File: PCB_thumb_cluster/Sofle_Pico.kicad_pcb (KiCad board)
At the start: 2 copper layers, 50 x 57.5 mm, 9 parts, among them J3 Conn_01x06, SW1 SW_PUSH, SW2 SW_PUSH, SW3 SW_PUSH, SW4 SW_PUSH

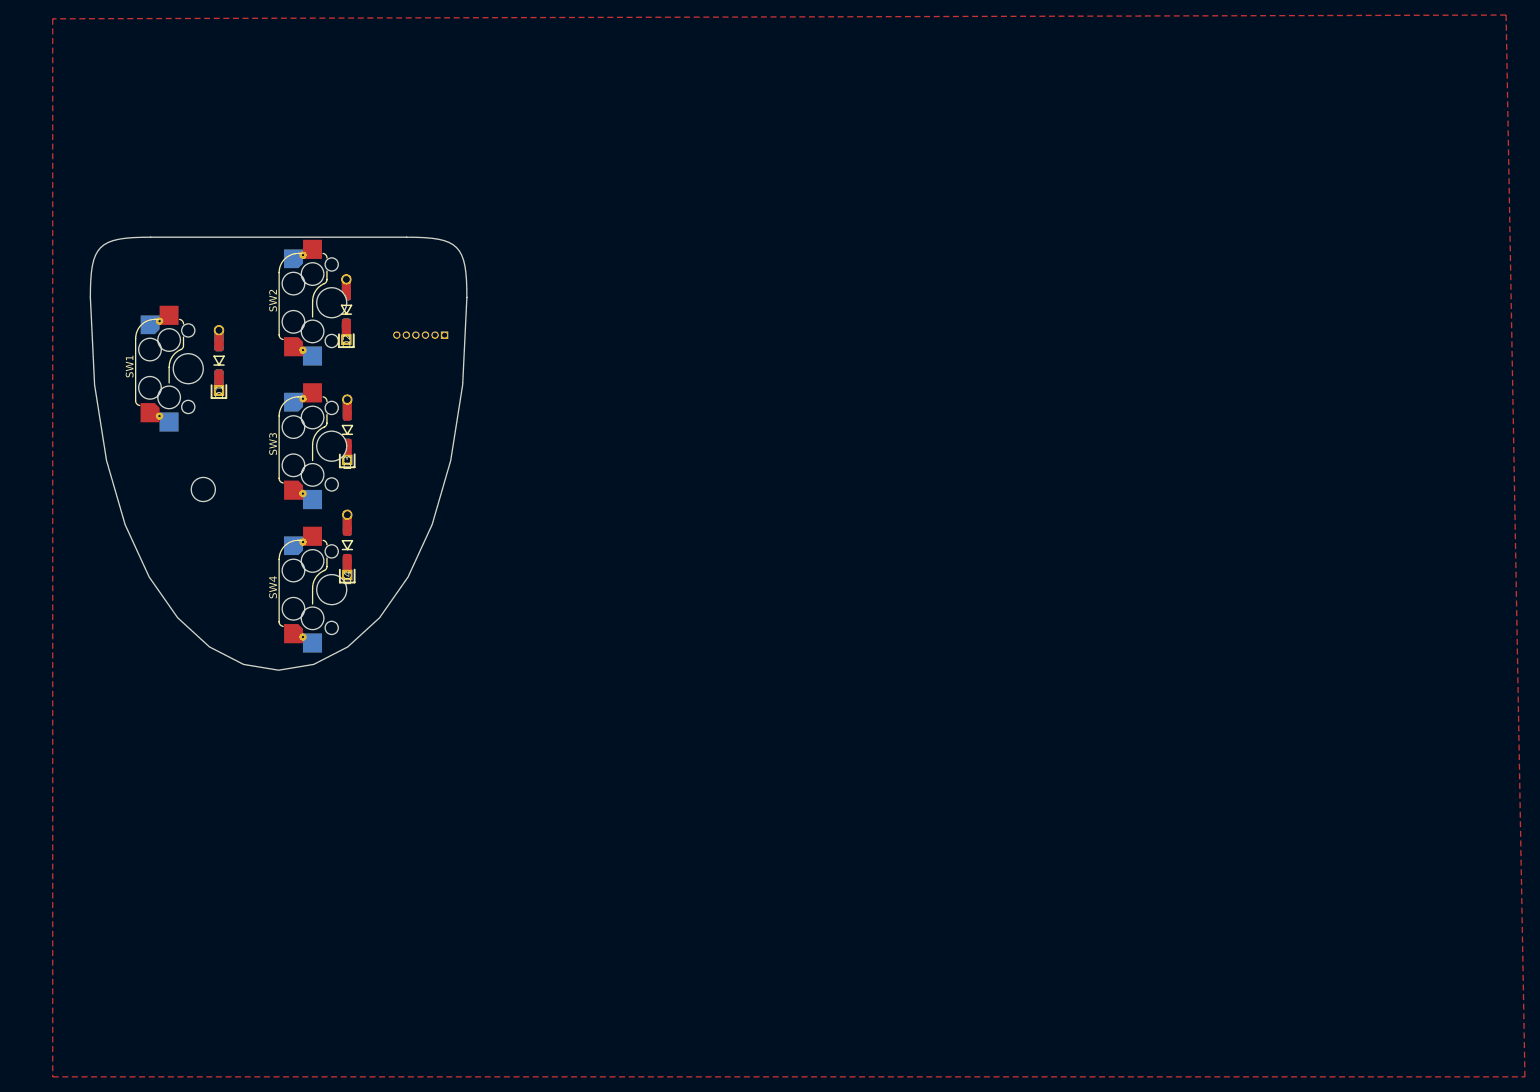
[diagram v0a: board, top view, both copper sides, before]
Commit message: route thumb cluster
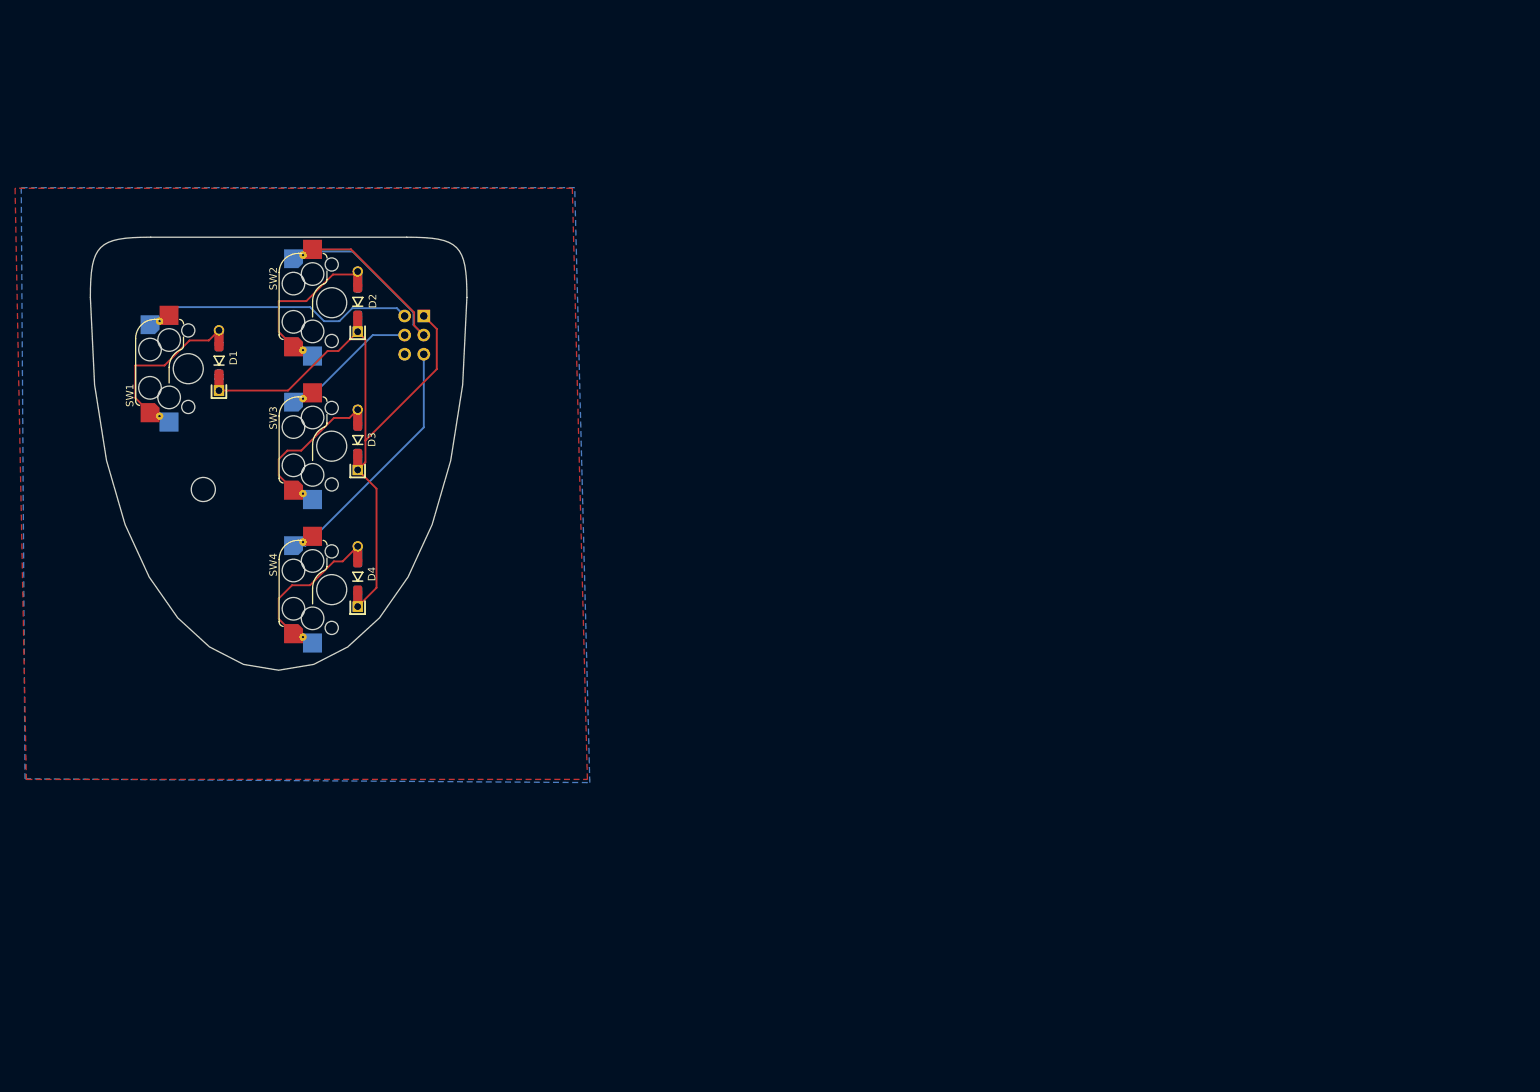
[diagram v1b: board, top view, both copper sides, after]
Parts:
- J3: value Conn_01x06 -> Conn_02x03; footprint Connector_PinHeader_1.27mm:PinHeader_1x06_P1.27mm_Horizontal -> Connector_PinHeader_2.54mm:PinHeader_2x03_P2.54mm_Vertical
- moved D4 4.41 mm to (106.5, 79.0)
- moved J3 3.75 mm to (115.3, 44.5), turned to 180 degrees
- moved D3 1.92 mm to (106.5, 60.9)
- moved D2 1.83 mm to (106.5, 42.5)
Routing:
- net row5: track 0.00 -> 82.3 mm
- net lcol1: track 0.00 -> 42.3 mm
- net lcol0: track 0.00 -> 35.2 mm
- net lcol3: track 0.00 -> 33.5 mm
- net Net-(D1-A): track 0.00 -> 20.1 mm
- net Net-(D2-A): track 0.00 -> 19.0 mm
- net Net-(D4-A): track 0.00 -> 18.8 mm
- net Net-(D3-A): track 0.00 -> 18.1 mm
- net lcol2: track 0.00 -> 17.0 mm
- added copper zone on B.Cu, net (none)
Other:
- board text removed: "USB"

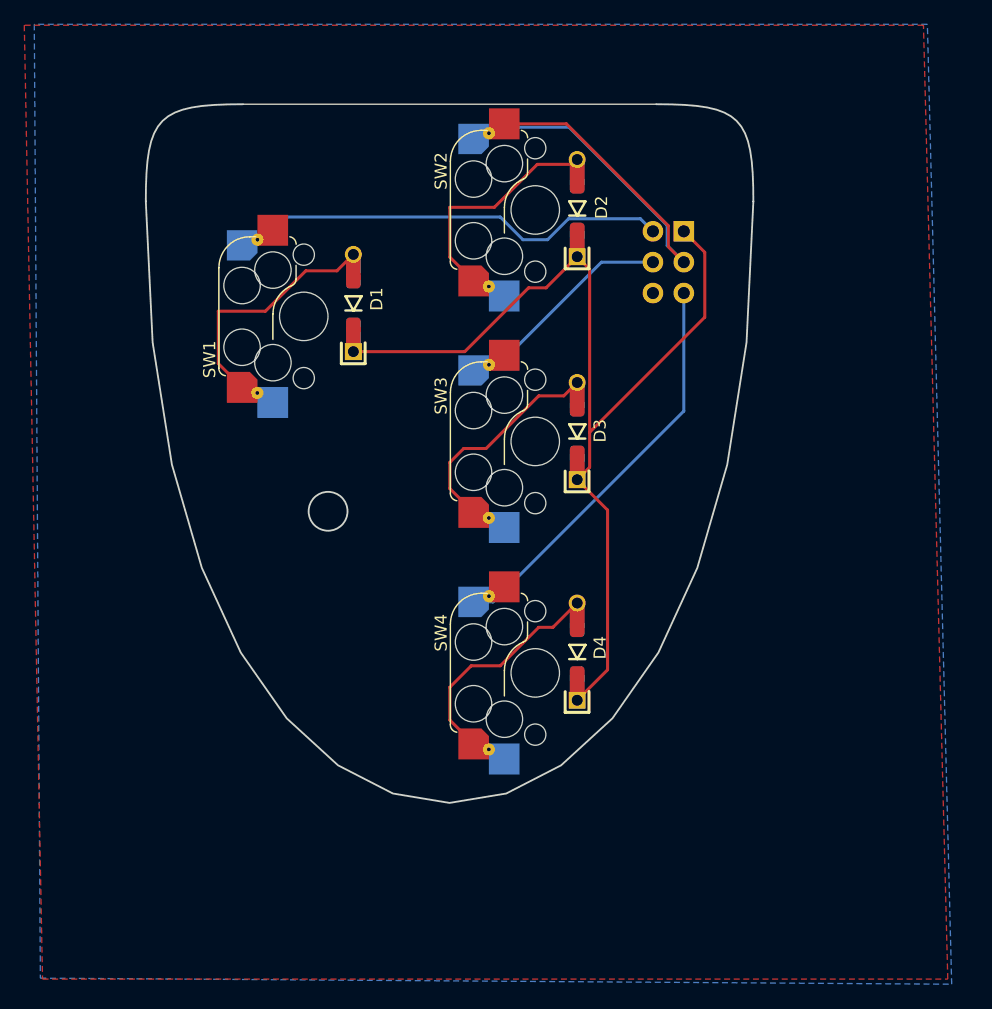
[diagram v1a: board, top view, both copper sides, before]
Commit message: relayout thumbcluster
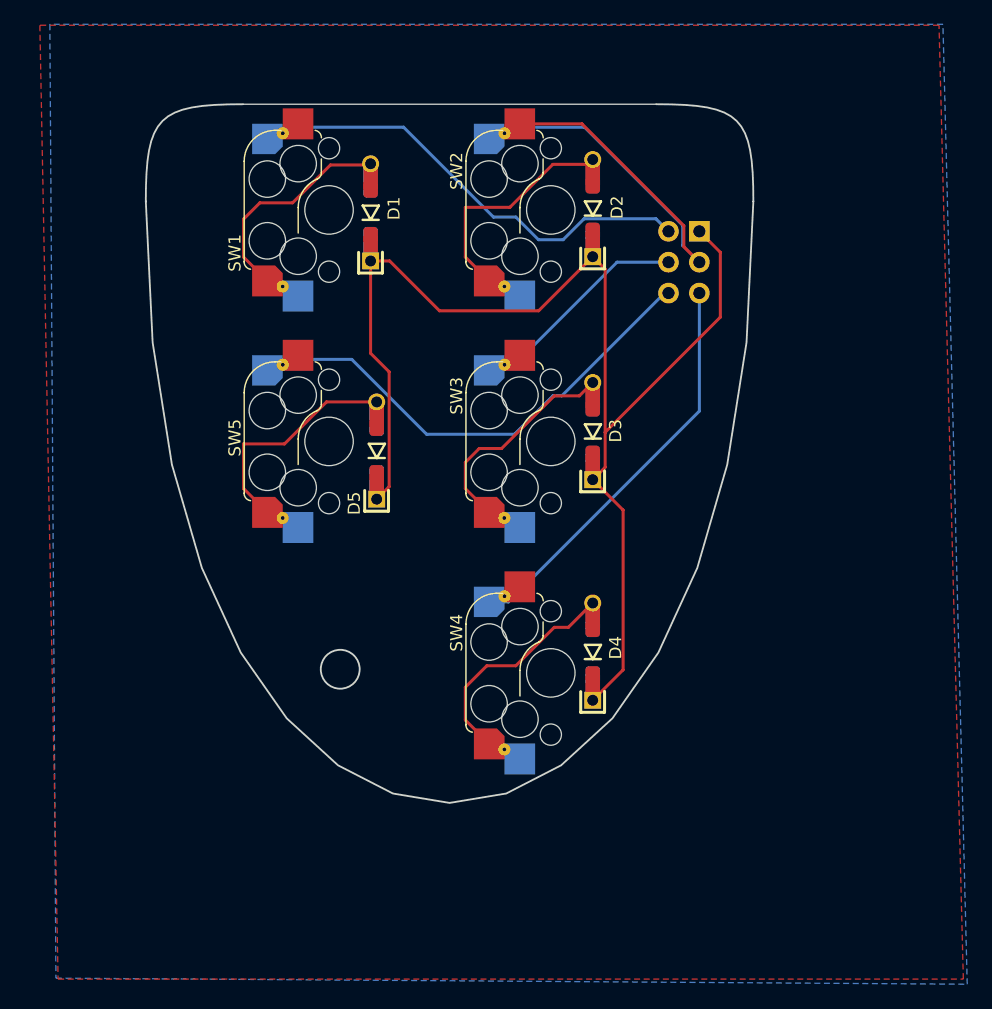
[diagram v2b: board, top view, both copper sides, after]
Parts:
- added D5: D, Sofle_Pico:D_SOD-123_DO-35_Hybrid_DoubleSided_V2, B.Cu at (90.0, 62.5)
- added SW5: SW_PUSH, Sofle_Pico:Cherry_MX_DS_Hotswap_v3.5.4, B.Cu at (86.1, 61.8)
- moved SW1 9.00 mm to (86.1, 42.7)
- moved D1 7.59 mm to (89.5, 42.9)
- moved D2 1.28 mm to (107.8, 42.5)
- moved D3 1.28 mm to (107.8, 60.9)
- moved D4 1.28 mm to (107.8, 79.0)
- moved J3 1.28 mm to (116.6, 44.5)
- moved SW2 1.28 mm to (104.3, 42.7)
- moved SW3 1.28 mm to (104.3, 61.8)
- moved SW4 1.28 mm to (104.3, 80.8)
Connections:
- J3 pad 6: unconnected-(J3-Pin_6-Pad6) -> lcol4
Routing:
- net lcol4: track 0.00 -> 40.8 mm
- net row5: track 82.3 -> 103.1 mm
- net Net-(D5-A): track 0.00 -> 18.8 mm
- net Net-(D1-A): track 20.1 -> 18.2 mm
- net lcol0: track 35.2 -> 36.9 mm
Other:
- outline, holes or cut-outs redrawn

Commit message: thumb cluster connection uses idc
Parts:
- J3: footprint Connector_PinHeader_2.54mm:PinHeader_2x03_P2.54mm_Vertical -> Connector_PinHeader_2.00mm:PinHeader_2x03_P2.00mm_Vertical
- moved J3 2.08 mm to (116.0, 42.5)
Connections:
- J3 pad 1: row5 -> lcol0
- J3 pad 2: lcol0 -> lcol1
- J3 pad 3: lcol1 -> lcol2
- J3 pad 4: lcol2 -> lcol3
- J3 pad 5: lcol3 -> lcol4
- J3 pad 6: lcol4 -> row5
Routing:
- net lcol1: track 42.3 -> 16.4 mm
- net row5: track 103.1 -> 88.2 mm
- net lcol3: track 33.5 -> 43.4 mm
- net lcol4: track 40.8 -> 49.9 mm
- net lcol2: track 17.0 -> 22.7 mm
- net lcol0: track 36.9 -> 39.3 mm
